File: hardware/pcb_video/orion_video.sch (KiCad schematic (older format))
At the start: 95 parts, among them J1 VGA, J2 SYSTEM, J4 MEM1, J5 MEM2, J6 VGAP, U1 AS7C4098A, U2 AS7C4098A, Y1 25MHz

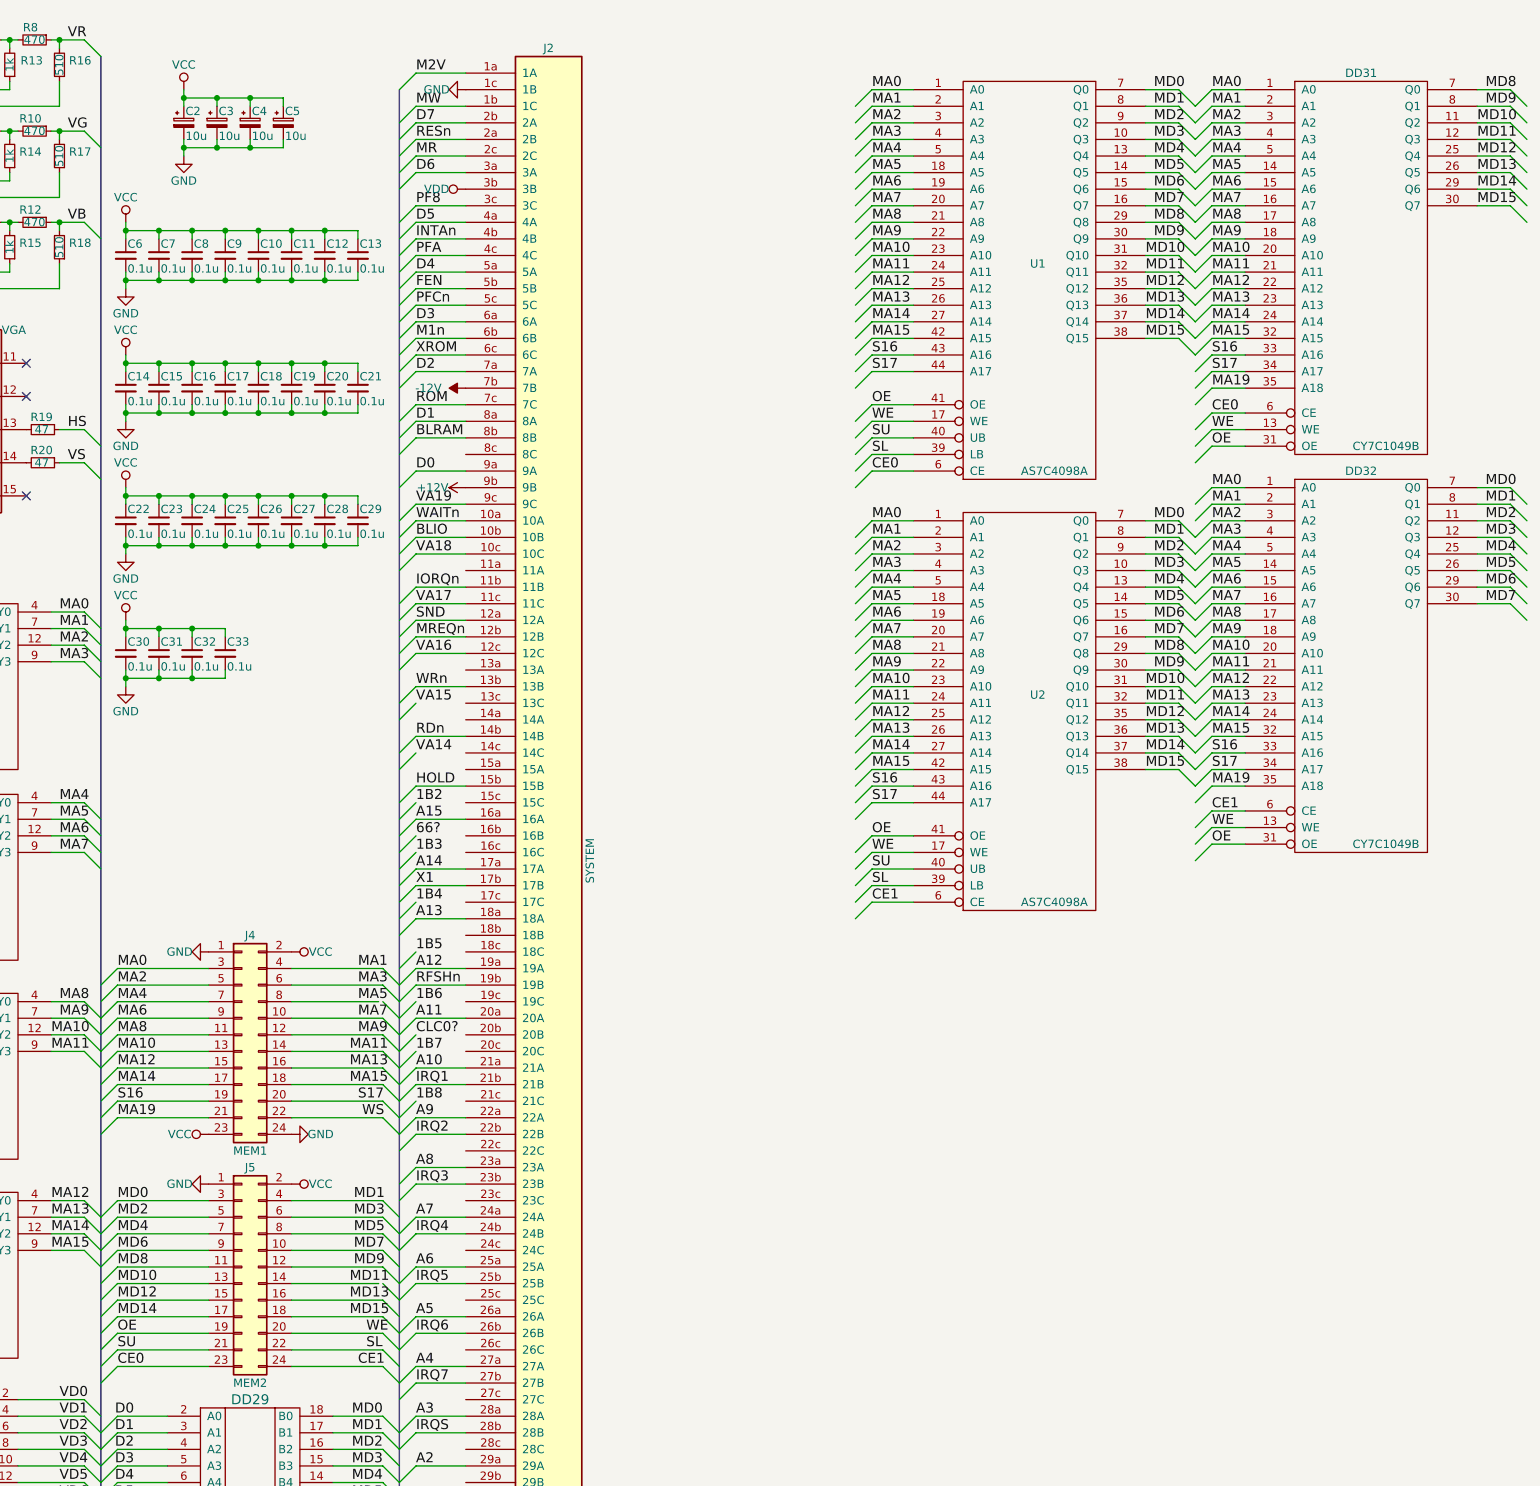
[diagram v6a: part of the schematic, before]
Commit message: Обновлено расположение компонентов, разъём SYSTEM заменён на 3-х рядный.
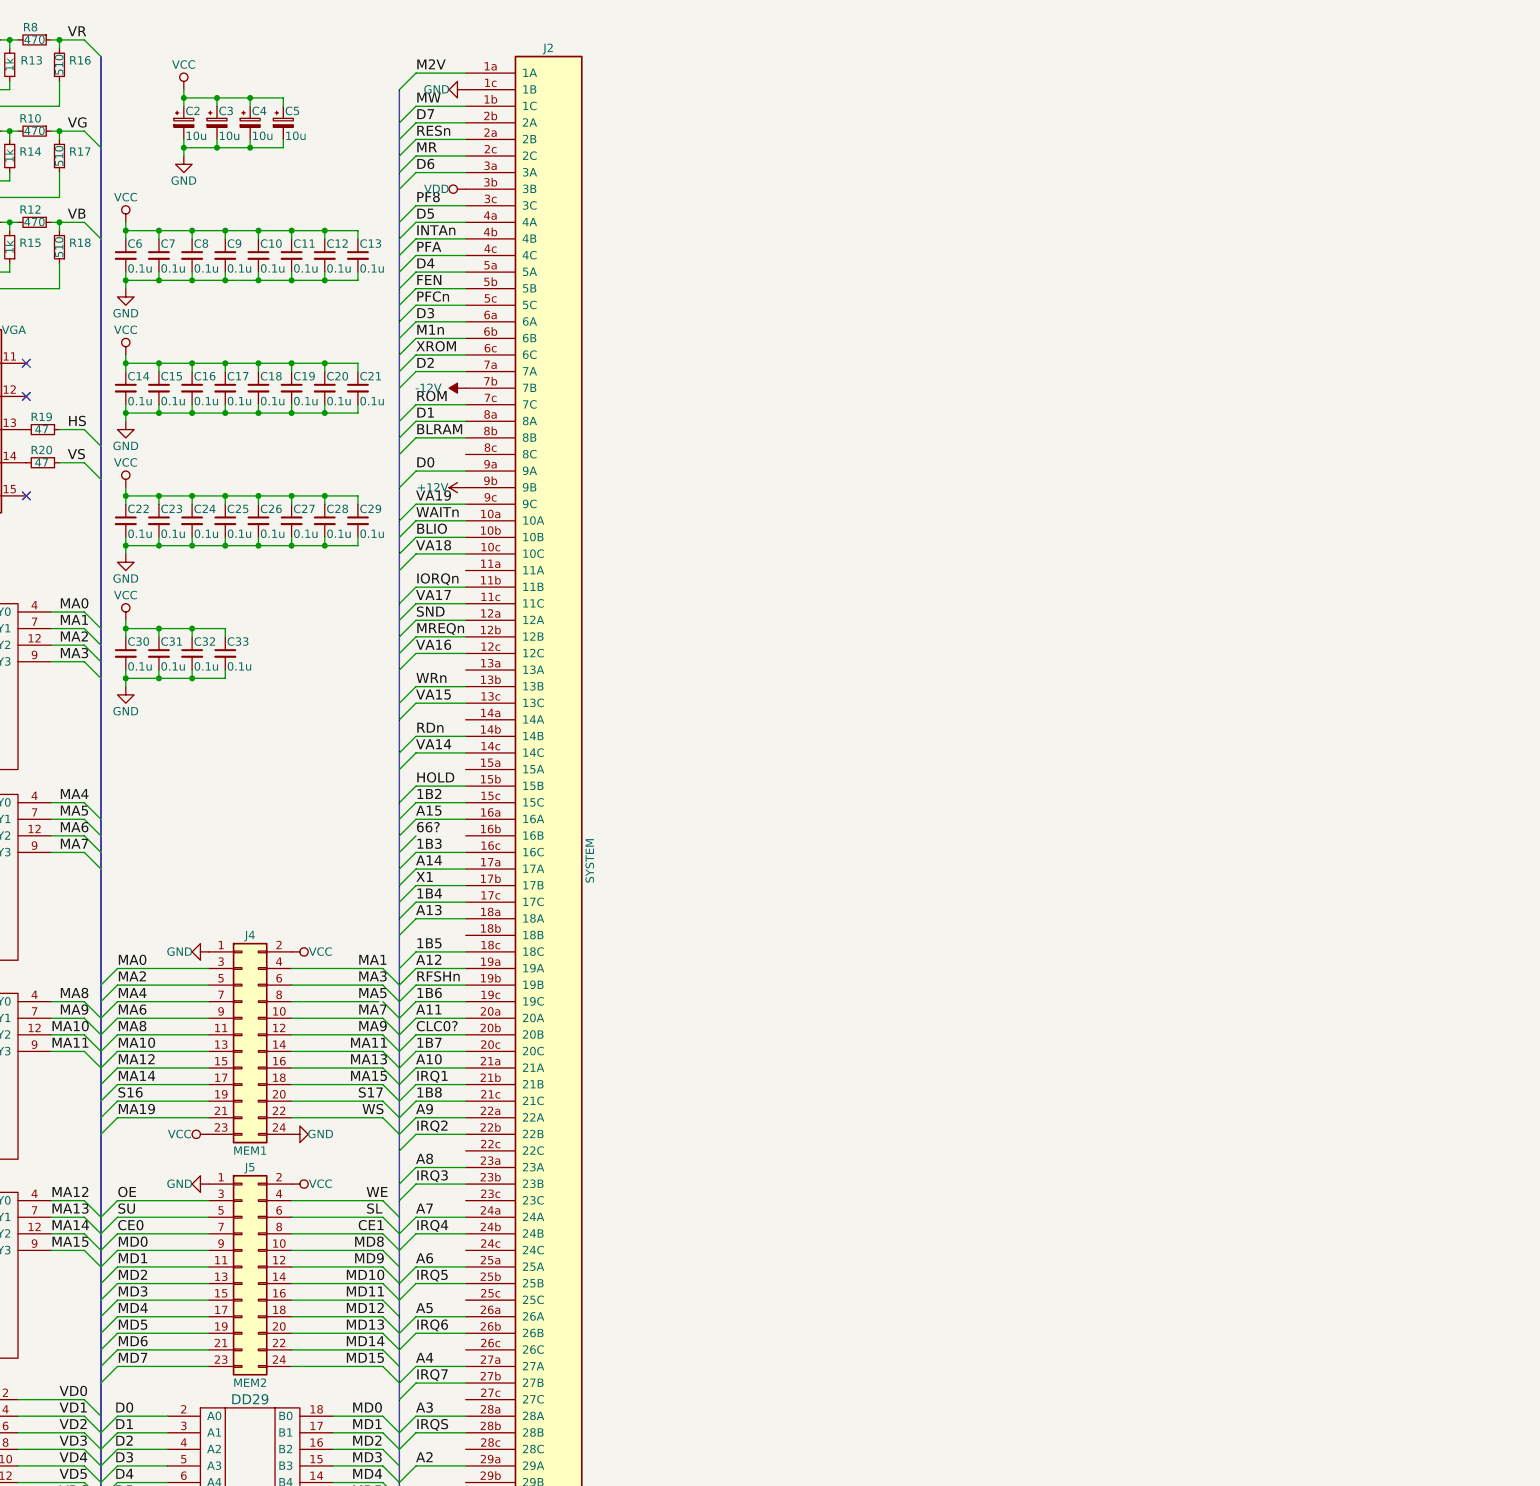
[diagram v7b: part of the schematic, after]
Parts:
- removed DD31, DD32: CY7C1049B, andreil:SOJ-36, symbol CY7C1049B
- removed U1, U2: AS7C4098A, andreil:SOJ-44, symbol AS7C4098A
- J4, J5: footprint Socket_Strips:Socket_Strip_Straight_2x12_Pitch2.00mm -> Socket_Strips:Socket_Strip_Straight_2x12_Pitch2.54mm
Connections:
- net 1B2: now also J2.15c (15C)
- net 1B3: now also J2.16c (16C)
- net 1B4: now also J2.17c (17C)
- net 1B5: now also J2.18c (18C)
- net 1B6: now also J2.19c (19C)
- net 1B7: now also J2.20c (20C)
- net 1B8: now also J2.21c (21C)
- net CE0: now also J5.7 (Pin_7); no longer J5.23 (Pin_23)
- net CE1: now also J5.8 (Pin_8); no longer J5.24 (Pin_24)
- net CLC0?: now also J2.20b (20B)
- net MD0: now also J5.9 (Pin_9); no longer J5.3 (Pin_3)
- net MD1: now also J5.11 (Pin_11); no longer J5.4 (Pin_4)
- net MD10: now also J5.14 (Pin_14); no longer J5.13 (Pin_13)
- net MD11: now also J5.16 (Pin_16); no longer J5.14 (Pin_14)
- net MD12: now also J5.18 (Pin_18); no longer J5.15 (Pin_15)
- net MD13: now also J5.20 (Pin_20); no longer J5.16 (Pin_16)
- net MD14: now also J5.22 (Pin_22); no longer J5.17 (Pin_17)
- net MD15: now also J5.24 (Pin_24); no longer J5.18 (Pin_18)
- net MD2: now also J5.13 (Pin_13); no longer J5.5 (Pin_5)
- net MD3: now also J5.15 (Pin_15); no longer J5.6 (Pin_6)
- net MD4: now also J5.17 (Pin_17); no longer J5.7 (Pin_7)
- net MD5: now also J5.19 (Pin_19); no longer J5.8 (Pin_8)
- net MD6: now also J5.21 (Pin_21); no longer J5.9 (Pin_9)
- net MD7: now also J5.23 (Pin_23); no longer J5.10 (Pin_10)
- net MD8: now also J5.10 (Pin_10); no longer J5.11 (Pin_11)
- net OE: now also J5.3 (Pin_3); no longer J5.19 (Pin_19)
- net SL: now also J5.6 (Pin_6); no longer J5.22 (Pin_22)
- net SU: now also J5.5 (Pin_5); no longer J5.21 (Pin_21)
- net VA14: now also J2.14c (14C)
- net VA15: now also J2.13c (13C)
- net WE: now also J5.4 (Pin_4); no longer J5.20 (Pin_20)
